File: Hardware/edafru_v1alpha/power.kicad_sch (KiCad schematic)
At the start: 0 parts

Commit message: all need circuits included to the schematic. ready for pcb component placement.
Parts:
- added C1: 10uF, Capacitor_SMD:C_1206_3216Metric_Pad1.33x1.80mm_HandSolder, symbol Device:C
- added C2: 220uF, Capacitor_Tantalum_SMD:CP_EIA-7343-30_AVX-N, symbol Device:C_Polarized
- added C3: 470uF, Capacitor_SMD:CP_Elec_10x10, symbol Device:C_Polarized
- added C4, C5, C9: 100nF, Capacitor_SMD:C_1206_3216Metric_Pad1.33x1.80mm_HandSolder, symbol Device:C
- added C6: 10nF, Capacitor_SMD:C_1206_3216Metric_Pad1.33x1.80mm_HandSolder, symbol Device:C
- added C7, C8: 1nF, Capacitor_SMD:C_1206_3216Metric_Pad1.33x1.80mm_HandSolder, symbol Device:C
- added D1: SMAJ18A, Diode_SMD:D_SMA, symbol Diode:SMAJ18A
- added D2: SS16T3G, Diode_SMD:D_SMA, symbol Diode:SS34
- added F1: 3A_Slow_Blow, Fuse:Fuse_1206_3216Metric_Pad1.42x1.75mm_HandSolder, symbol Device:Fuse
- added FB1: 10R, Inductor_SMD:L_1206_3216Metric_Pad1.22x1.90mm_HandSolder, symbol Device:FerriteBead
- added L1, L2: 47uH, Inductor_SMD:L_1210_3225Metric_Pad1.42x2.65mm_HandSolder, symbol Device:L
- added R1: 2R2, Resistor_SMD:R_1206_3216Metric_Pad1.30x1.75mm_HandSolder, symbol Device:R
- added R2: 0R, Resistor_SMD:R_1206_3216Metric_Pad1.30x1.75mm_HandSolder, symbol Device:R
- added U1: TLF80511TFV50, Package_TO_SOT_SMD:TO-252-2, symbol Regulator_Linear:L7805
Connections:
- new net: D2.1 (K), F1.1
- new net: C3.1, F1.2, L2.1
- new net: C4.1, C6.1, C7.1, FB1.1, L1.2
- new net: C5.2, R1.1
- new net +12P: C1.1, C5.1, C8.1, L2.2, U1.1 (IN)
- new net +5V: C2.1, L1.1, U1.3 (OUT)
- new net +BATT: D1.1 (A1), D2.2 (A)
- new net -BATT: C3.2, D1.2 (A2), R1.2, R2.1
- new net GND: C1.2, C2.2, C4.2, C6.2, C7.2, C8.2, C9.2, R2.2, U1.2 (GND)
- new net VCC: C9.1, FB1.2
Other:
- note added: "JUMPER"
- note added: "POWER INPUT"
- note added: "VOLTAGE REGULATOR"

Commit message: PCB is developing...
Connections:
- net +12P: no longer C5.1
- net +BATT: now also F1.2; no longer D2.2 (A)
- net at F1.1: now also D2.2 (A); no longer D2.1 (K)
- net at C3.1, L2.1: now also C5.1, D2.1 (K); no longer F1.2
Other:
- moved on the sheet: D2, F1, L2, R2

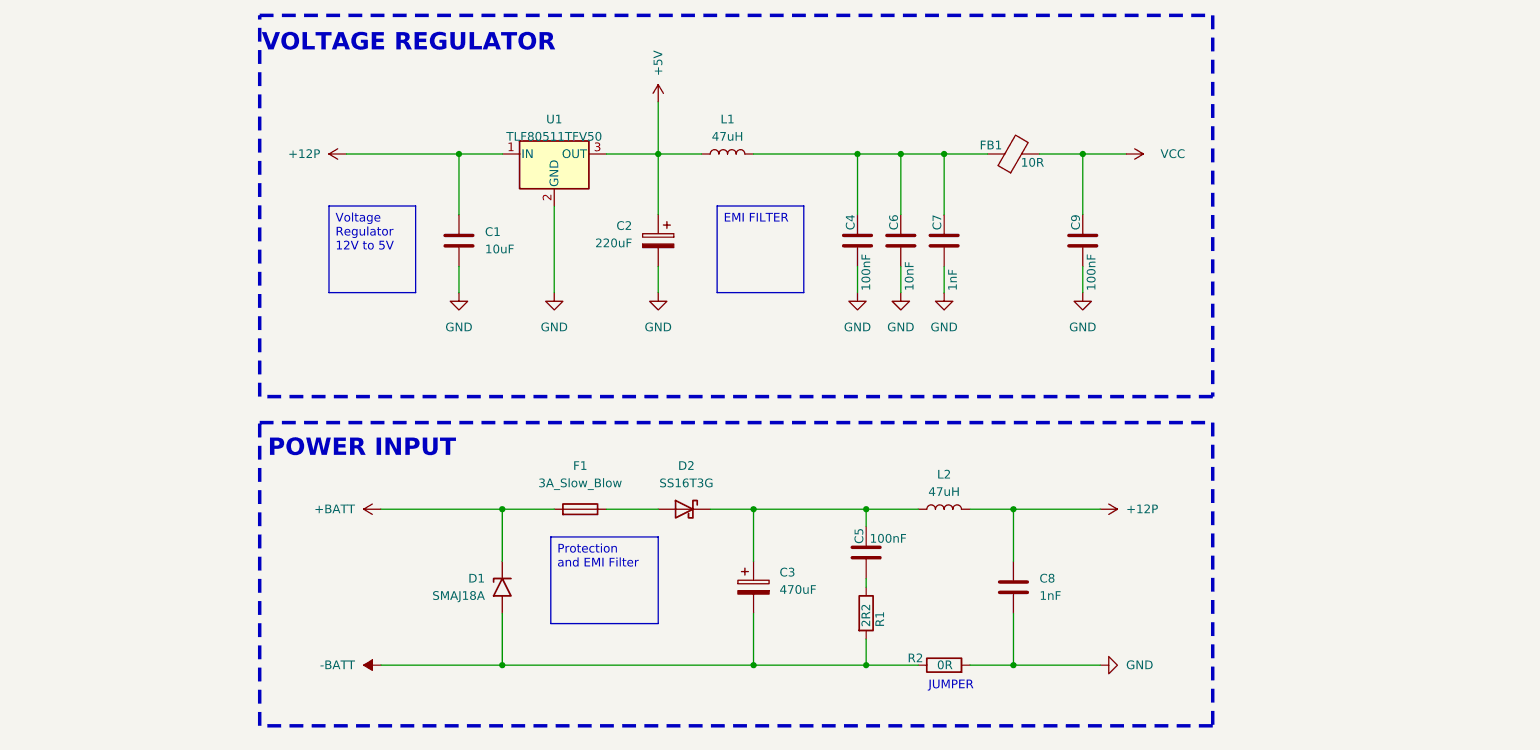
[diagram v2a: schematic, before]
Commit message: developement is stopped depend on new EDVDU.
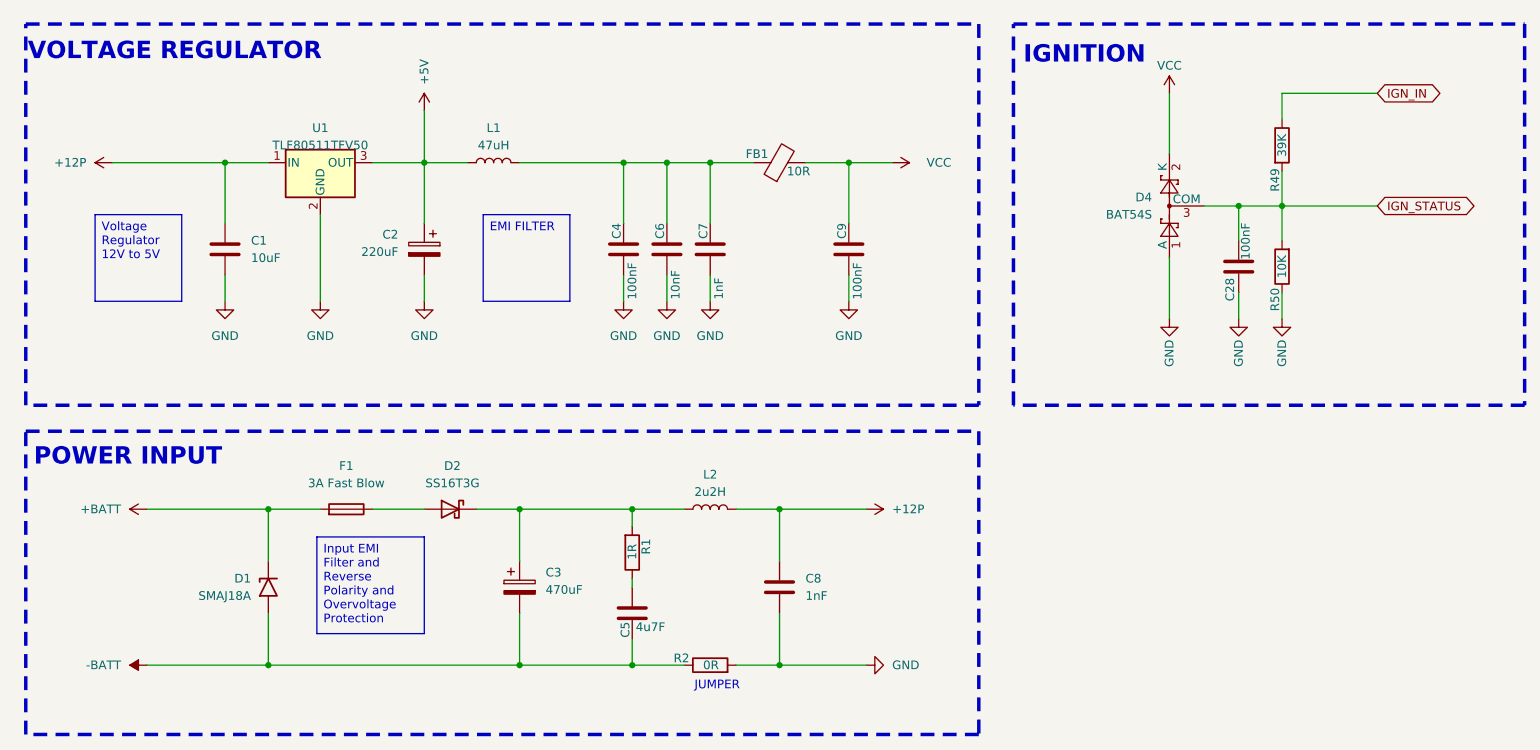
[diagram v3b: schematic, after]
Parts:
- added C28: 100nF, Capacitor_SMD:C_0603_1608Metric_Pad1.08x0.95mm_HandSolder, symbol Device:C
- added D4: BAT54S, Package_TO_SOT_SMD:SOT-23, symbol Diode:BAT54S
- added R49: 39K, Resistor_SMD:R_0603_1608Metric_Pad0.98x0.95mm_HandSolder, symbol Device:R
- added R50: 10K, Resistor_SMD:R_0603_1608Metric_Pad0.98x0.95mm_HandSolder, symbol Device:R
- C5: value 100nF -> 4u7F
- F1: value 3A_Slow_Blow -> 3A Fast Blow
- L2: value 47uH -> 2u2H
- R1: value 2R2 -> 1R
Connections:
- net -BATT: now also C5.1; no longer R1.2
- net GND: now also C28.2, D4.1 (A), R50.1
- net VCC: now also D4.2 (K)
- net at C3.1, D2.1 (K), L2.1: now also R1.2; no longer C5.1
- new net IGN_IN: R49.1
- new net IGN_STATUS: C28.1, D4.3 (COM), R49.2, R50.2
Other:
- note added: "IGNITION"
- moved on the sheet: C1, C2, C3, C4, C6, C7, C8, C9, D1, D2, F1, FB1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
